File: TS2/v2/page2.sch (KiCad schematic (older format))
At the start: 6 parts, among them U10 74LS32, U19 74LS20, U24 74LS260, U25 74LS260, U26 74LS138, U27 25LS2548

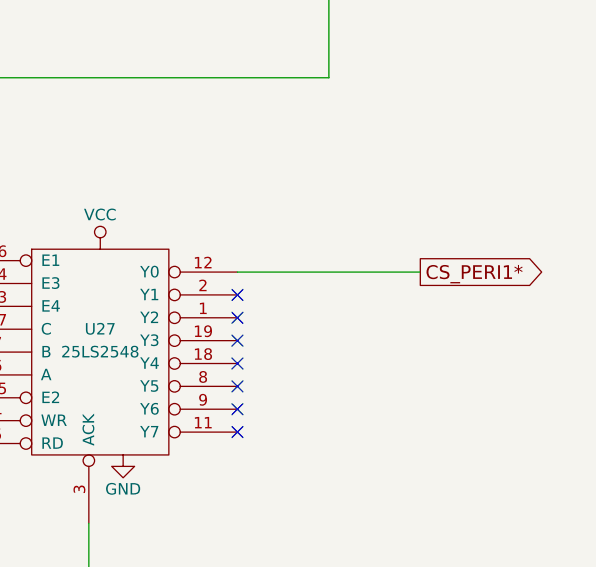
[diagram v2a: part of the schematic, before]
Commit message: Fixed error in original schematic. Prototype board is up and running.
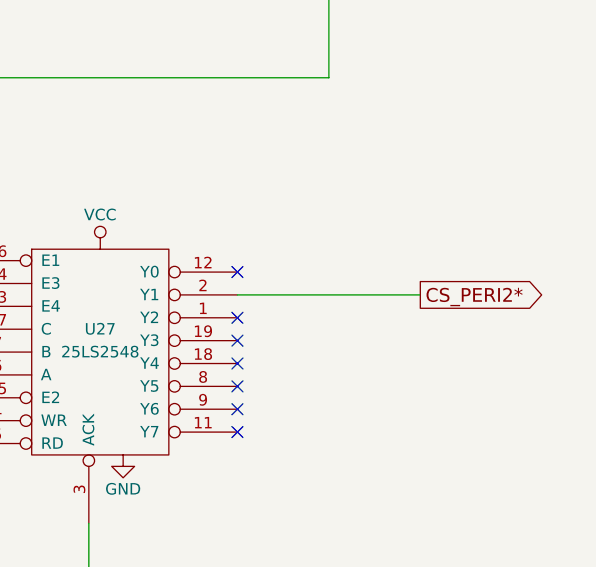
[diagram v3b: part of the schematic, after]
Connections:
- net CS_PERI2*: now reaches U27.2 (Y1)
- net CS_PERI1*: no longer names the net of U27.12 (Y0)
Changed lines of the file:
@@
 Sheet 3 9
 Title "TS2 68000 Single Board Computer"
-Date "2016-12-31"
+Date "2017-01-03"
 Rev "2.0"
 Comp "Jeff Tranter"
@@
 NoConn ~ 8500 2100
 $Comp
-L GND #PWR032
+L GND #PWR034
 U 1 1 57C1E00A
 P 7900 2200
-F 0 "#PWR032" H 7900 1950 50  0001 C CNN
+F 0 "#PWR034" H 7900 1950 50  0001 C CNN
 F 1 "GND" H 7900 2050 50  0000 C CNN
 F 2 "" H 7900 2200 50  0000 C CNN
@@
 $EndComp
 $Comp
-L VCC #PWR033
+L VCC #PWR035
 U 1 1 57C1E030
 P 7900 1300
-F 0 "#PWR033" H 7900 1150 50  0001 C CNN
+F 0 "#PWR035" H 7900 1150 50  0001 C CNN
 F 1 "VCC" H 7900 1450 50  0000 C CNN
 F 2 "" H 7900 1300 50  0000 C CNN
@@
 Wire Wire Line
 	8900 2900 8900 1800
-Wire Wire Line
-	8500 3750 9300 3750
-Text GLabel 9300 3750 2    60   Output ~ 0
-CS_PERI1*
+Text GLabel 9300 3850 2    60   Output ~ 0
+CS_PERI2*
 NoConn ~ 8500 4050
 NoConn ~ 8500 4150
@@
 NoConn ~ 8500 4450
 $Comp
-L GND #PWR034
+L GND #PWR036
 U 1 1 57C1E717
 P 8000 4550
-F 0 "#PWR034" H 8000 4300 50  0001 C CNN
+F 0 "#PWR036" H 8000 4300 50  0001 C CNN
 F 1 "GND" H 8000 4400 50  0000 C CNN
 F 2 "" H 8000 4550 50  0000 C CNN
@@
 $EndComp
 $Comp
-L VCC #PWR035
+L VCC #PWR037
 U 1 1 57C1E73D
 P 7900 3650
-F 0 "#PWR035" H 7900 3500 50  0001 C CNN
+F 0 "#PWR037" H 7900 3500 50  0001 C CNN
 F 1 "VCC" H 7900 3800 50  0000 C CNN
 F 2 "" H 7900 3650 50  0000 C CNN
@@
 	7200 3900 7200 3700
 $Comp
-L VCC #PWR036
+L VCC #PWR038
 U 1 1 57C1EB1C
 P 7200 3700
-F 0 "#PWR036" H 7200 3550 50  0001 C CNN
+F 0 "#PWR038" H 7200 3550 50  0001 C CNN
 F 1 "VCC" H 7200 3850 50  0000 C CNN
 F 2 "" H 7200 3700 50  0000 C CNN
@@
 Wire Wire Line
 	8900 1800 8500 1800
-NoConn ~ 8500 3850
 NoConn ~ 8500 3950
 Wire Wire Line
 	7850 6200 1150 6200
+NoConn ~ 8500 3750
+Wire Wire Line
+	8500 3850 9300 3850
 $EndSCHEMATC
